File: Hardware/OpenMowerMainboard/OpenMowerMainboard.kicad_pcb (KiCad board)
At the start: 2 copper layers, 180 x 170 mm, 177 parts, among them IC1 74ALVC164245DGG,11, IC2 TSC101CILT, IC3 MAX20405AFOF_VY+T, J1 Conn_02x11_Top_Bottom, J10 Conn_01x05, J11 Conn_01x03_Male, J12 Conn_01x03_Male, J13 Conn_01x03_Male, J14 Conn_01x03_Male, J16 Conn_01x08, J17 Conn_01x02, J18 Conn_01x02, J19 Conn_01x04, J2 Conn_02x04_Top_Bottom, J20 Conn_01x10_Female, J21 Raspberry_Pi_2_3, J22 Conn_02x04_Odd_Even, J23 Conn_01x08, J3 Conn_01x02, J4 Conn_01x05, J5 Conn_01x04, J6 Conn_01x04, J7 Conn_01x04, J8 Conn_01x04, J9 Conn_01x04, M1 Fan, Q13 BSS138, Q14 BSS138, Q15 BSS138, Q16 BSS138, Q3 BSS138, Q5 BSS138, Q6 Q_PMOS_GDS, SW1 MK-11C04-G013, SW2 DA-01BP, U1 DNP, U10 74HC4051, U11 Pico, U2 MCP604, U3 SIP32509DT, U4 xESC2, U5 xESC2, U6 xESC2, U7 SN74LV1T34DBV, U9 74HC4051

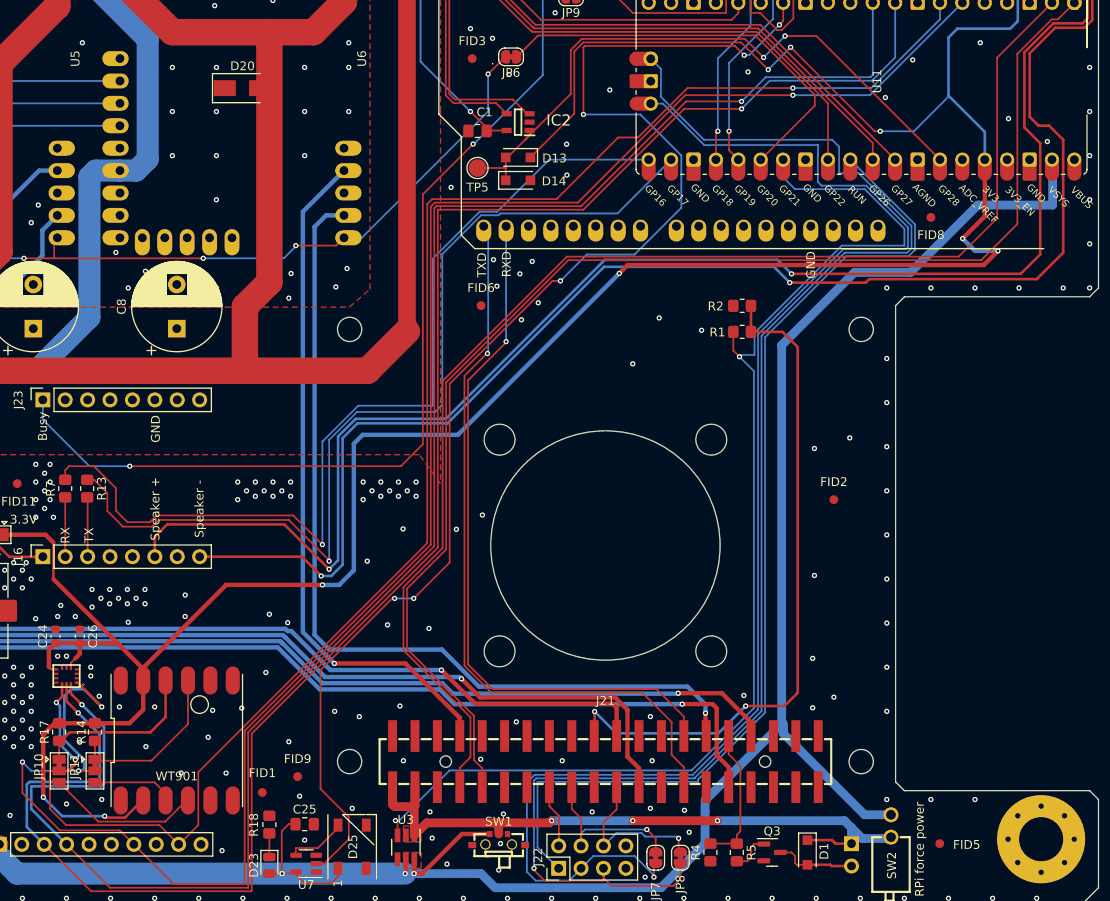
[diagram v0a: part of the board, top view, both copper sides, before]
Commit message: feat: add F1 PPTC for 3.3V rail
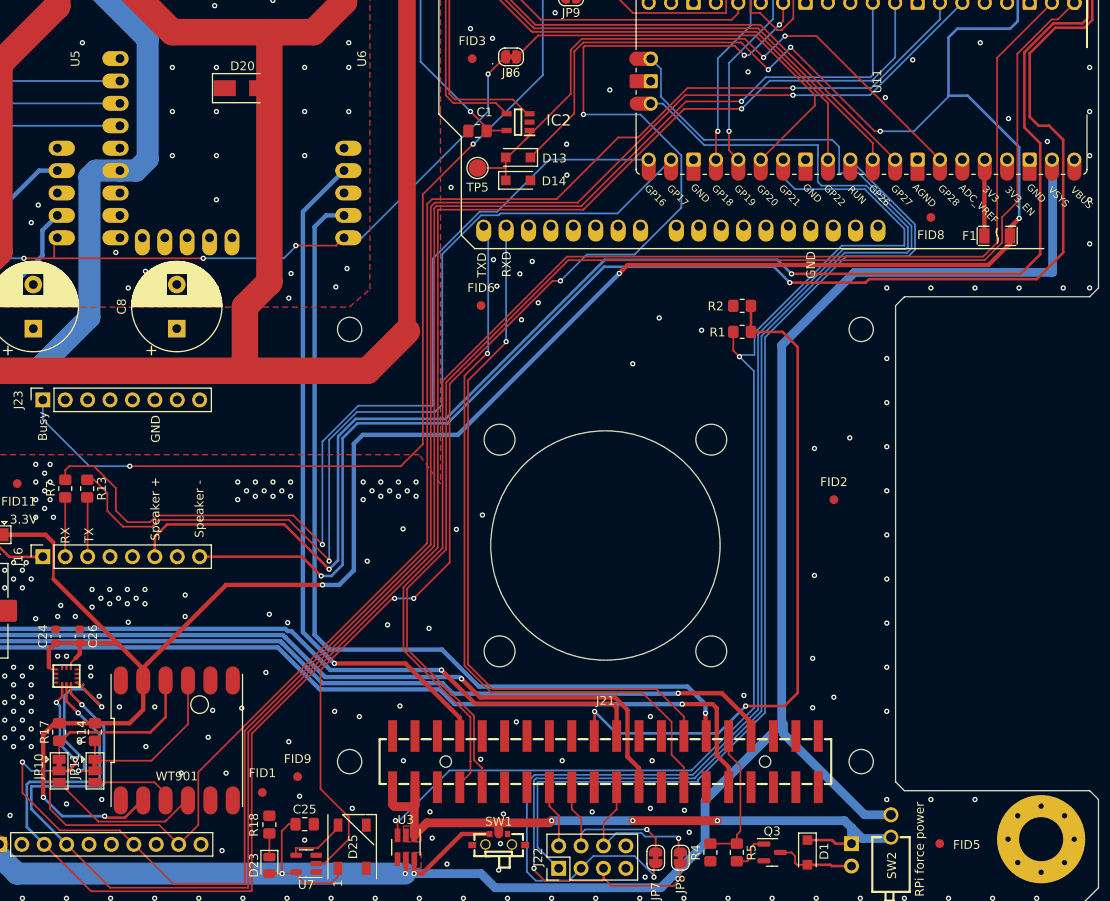
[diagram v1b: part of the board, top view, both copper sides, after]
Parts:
- added F1: nSMD035-16V, lcsc:F1206, F.Cu at (188.5, 114.1)
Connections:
- U11 pad 36: +3V3 -> Net-(U11-3V3)
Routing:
- net Net-(U11-3V3): track 0.00 -> 7.06 mm
- net +5V: track 882.8 -> 887.2 mm
- net /RaspberryPi/UART0_TXD: track 148.7 -> 150.3 mm
- net +3V3: vias 19 -> 18

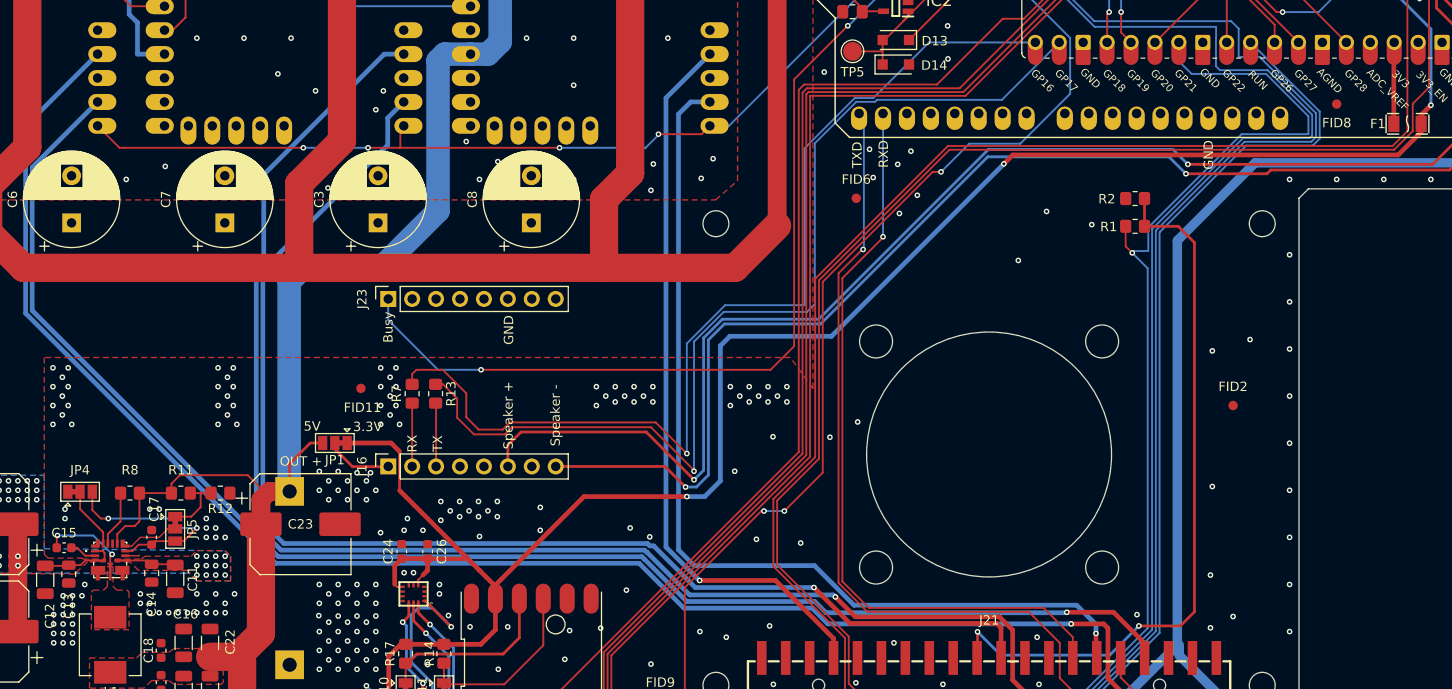
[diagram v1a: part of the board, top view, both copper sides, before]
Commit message: feat: bigger pads and thermal relief for MAX2040
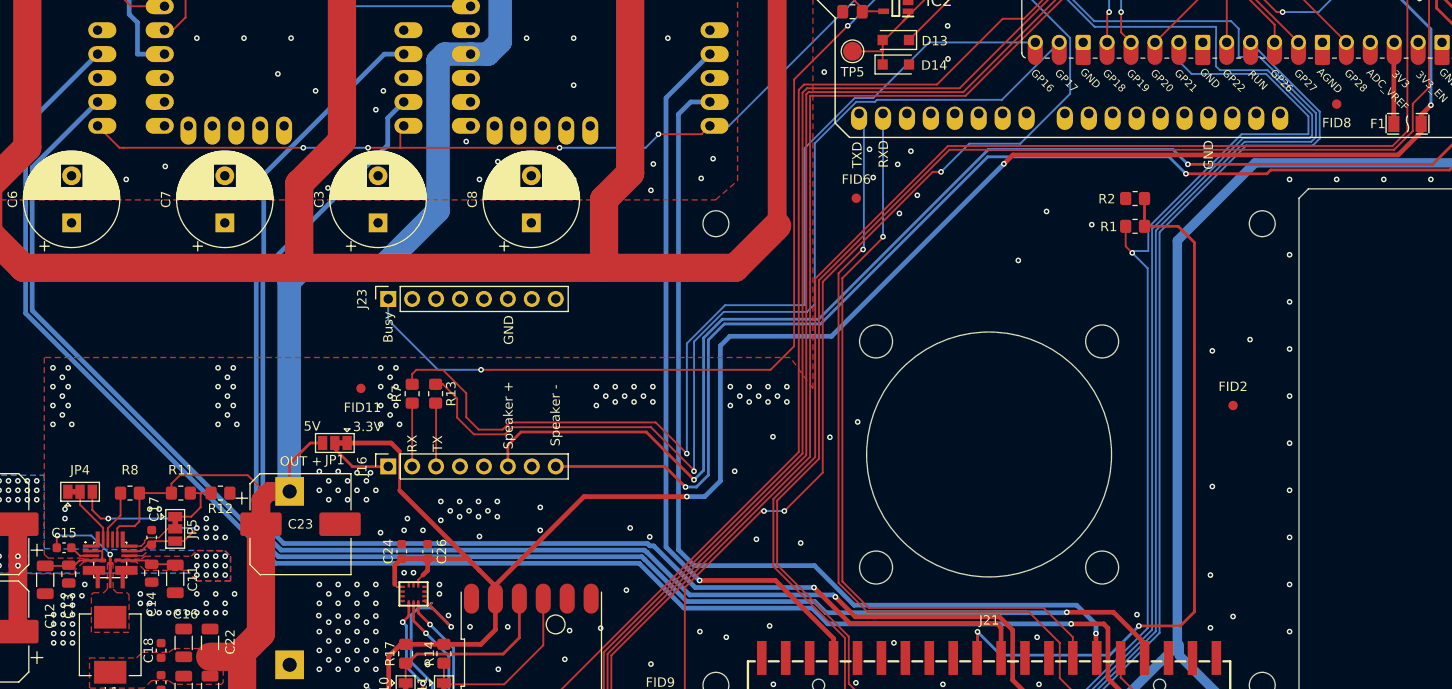
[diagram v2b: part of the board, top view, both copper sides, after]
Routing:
- net GND: track 2.92 -> 3.75 mm
